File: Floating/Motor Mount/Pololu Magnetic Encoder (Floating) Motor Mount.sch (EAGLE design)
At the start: 1 part

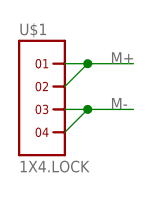
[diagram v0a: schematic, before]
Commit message: Added decoupling capacitor to motor connetions Made 'oval' vias for motors
All in all, should now fit motors
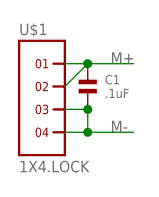
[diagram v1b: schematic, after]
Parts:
- added C1: .1uF, standardparts:CAPACITOR.0603
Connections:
- net M+: now also C1.1
- net M-: now also C1.2
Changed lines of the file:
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@@
 <setting verticaltext="up"/>
 </settings>
-<grid distance="25" unitdist="mil" unit="mil" style="dots" multiple="2" display="yes" altdistance="5" altunitdist="mil" altunit="mil"/>
+<grid distance="0.1" unitdist="inch" unit="inch" style="lines" multiple="1" display="no" altdistance="0.01" altunitdist="inch" altunit="inch"/>
 <layers>
-<layer number="1" name="Top" color="4" fill="1" visible="yes" active="no"/>
-<layer number="16" name="Bottom" color="1" fill="1" visible="yes" active="no"/>
-<layer number="17" name="Pads" color="2" fill="1" visible="yes" active="no"/>
-<layer number="18" name="Vias" color="2" fill="1" visible="yes" active="no"/>
-<layer number="19" name="Unrouted" color="6" fill="1" visible="yes" active="no"/>
-<layer number="20" name="Dimension" color="15" fill="1" visible="yes" active="no"/>
-<layer number="21" name="tPlace" color="7" fill="1" visible="yes" active="no"/>
-<layer number="22" name="bPlace" color="7" fill="1" visible="yes" active="no"/>
-<layer number="23" name="tOrigins" color="15" fill="1" visible="yes" active="no"/>
-<layer number="24" name="bOrigins" color="15" fill="1" visible="yes" active="no"/>
-<layer number="25" name="tNames" color="7" fill="1" visible="yes" active="no"/>
-<layer number="26" name="bNames" color="7" fill="1" visible="yes" active="no"/>
-<layer number="27" name="tValues" color="7" fill="1" visible="yes" active="no"/>
-<layer number="28" name="bValues" color="7" fill="1" visible="yes" active="no"/>
+<layer number="1" name="Top" color="4" fill="1" visible="no" active="no"/>
+<layer number="16" name="Bottom" color="1" fill="1" visible="no" active="no"/>
+<layer number="17" name="Pads" color="2" fill="1" visible="no" active="no"/>
+<layer number="18" name="Vias" color="2" fill="1" visible="no" active="no"/>
+<layer number="19" name="Unrouted" color="6" fill="1" visible="no" active="no"/>
+<layer number="20" name="Dimension" color="15" fill="1" visible="no" active="no"/>
+<layer number="21" name="tPlace" color="7" fill="1" visible="no" active="no"/>
+<layer number="22" name="bPlace" color="7" fill="1" visible="no" active="no"/>
+<layer number="23" name="tOrigins" color="15" fill="1" visible="no" active="no"/>
+<layer number="24" name="bOrigins" color="15" fill="1" visible="no" active="no"/>
+<layer number="25" name="tNames" color="7" fill="1" visible="no" active="no"/>
+<layer number="26" name="bNames" color="7" fill="1" visible="no" active="no"/>
+<layer number="27" name="tValues" color="7" fill="1" visible="no" active="no"/>
+<layer number="28" name="bValues" color="7" fill="1" visible="no" active="no"/>
 <layer number="29" name="tStop" color="7" fill="3" visible="no" active="no"/>
 <layer number="30" name="bStop" color="7" fill="6" visible="no" active="no"/>
@@
 <layer number="35" name="tGlue" color="7" fill="4" visible="no" active="no"/>
 <layer number="36" name="bGlue" color="7" fill="5" visible="no" active="no"/>
-<layer number="37" name="tTest" color="7" fill="1" visible="yes" active="no"/>
-<layer number="38" name="bTest" color="7" fill="1" visible="yes" active="no"/>
+<layer number="37" name="tTest" color="7" fill="1" visible="no" active="no"/>
+<layer number="38" name="bTest" color="7" fill="1" visible="no" active="no"/>
 <layer number="39" name="tKeepout" color="4" fill="11" visible="no" active="no"/>
 <layer number="40" name="bKeepout" color="1" fill="11" visible="no" active="no"/>
@@
 <layer number="44" name="Drills" color="7" fill="1" visible="no" active="no"/>
 <layer number="45" name="Holes" color="7" fill="1" visible="no" active="no"/>
-<layer number="46" name="Milling" color="3" fill="1" visible="yes" active="no"/>
-<layer number="47" name="Measures" color="7" fill="1" visible="yes" active="no"/>
-<layer number="48" name="Document" color="7" fill="1" visible="yes" active="no"/>
-<layer number="49" name="Reference" color="7" fill="1" visible="yes" active="no"/>
-<layer number="50" name="dxf" color="7" fill="1" visible="yes" active="no"/>
-<layer number="51" name="tDocu" color="7" fill="1" visible="yes" active="no"/>
-<layer number="52" name="bDocu" color="7" fill="1" visible="yes" active="no"/>
-<layer number="53" name="tGND_GNDA" color="7" fill="9" visible="yes" active="no"/>
-<layer number="54" name="bGND_GNDA" color="1" fill="9" visible="yes" active="no"/>
-<layer number="56" name="wert" color="7" fill="1" visible="yes" active="no"/>
+<layer number="46" name="Milling" color="3" fill="1" visible="no" active="no"/>
+<layer number="47" name="Measures" color="7" fill="1" visible="no" active="no"/>
+<layer number="48" name="Document" color="7" fill="1" visible="no" active="no"/>
+<layer number="49" name="Reference" color="7" fill="1" visible="no" active="no"/>
+<layer number="50" name="dxf" color="7" fill="1" visible="no" active="no"/>
+<layer number="51" name="tDocu" color="7" fill="1" visible="no" active="no"/>
+<layer number="52" name="bDocu" color="7" fill="1" visible="no" active="no"/>
+<layer number="53" name="tGND_GNDA" color="7" fill="9" visible="no" active="no"/>
+<layer number="54" name="bGND_GNDA" color="1" fill="9" visible="no" active="no"/>
+<layer number="56" name="wert" color="7" fill="1" visible="no" active="no"/>
 <layer number="91" name="Nets" color="2" fill="1" visible="yes" active="yes"/>
 <layer number="92" name="Busses" color="1" fill="1" visible="yes" active="yes"/>
@@
 <part name="U$10" library="thinkmaketest" deviceset="A4_LAYOUT" device=""/>
 <part name="U$1" library="headers(.05in)" deviceset="1X4" device=".LOCK"/>
+<part name="C1" library="standardparts" deviceset="CAPACITOR" device=".0603" value=".1uF"/>
 </parts>
 <sheets>
@@
 <instance part="U$10" gate="G$1" x="0" y="0"/>
 <instance part="U$1" gate="G$1" x="96.52" y="93.98"/>
+<instance part="C1" gate="G$1" x="101.6" y="96.52" rot="R270"/>
 </instances>
 <busses>
@@
 <pinref part="U$1" gate="G$1" pin="1"/>
 <pinref part="U$1" gate="G$1" pin="2"/>
+<pinref part="C1" gate="G$1" pin="1"/>
 </segment>
 </net>
 <net name="M-" class="0">
 <segment>
-<wire x1="99.06" y1="93.98" x2="101.6" y2="93.98" width="0.1524" layer="91"/>
-<wire x1="101.6" y1="93.98" x2="106.68" y2="93.98" width="0.1524" layer="91"/>
-<wire x1="99.06" y1="91.44" x2="101.6" y2="93.98" width="0.1524" layer="91"/>
-<junction x="101.6" y="93.98"/>
-<label x="104.14" y="93.98" size="1.27" layer="95"/>
+<label x="104.14" y="91.44" size="1.27" layer="95"/>
 <pinref part="U$1" gate="G$1" pin="3"/>
 <pinref part="U$1" gate="G$1" pin="4"/>
+<wire x1="106.68" y1="91.44" x2="101.6" y2="91.44" width="0.1524" layer="91"/>
+<wire x1="101.6" y1="91.44" x2="99.06" y2="91.44" width="0.1524" layer="91"/>
+<junction x="101.6" y="91.44"/>
+<pinref part="C1" gate="G$1" pin="2"/>
+<wire x1="101.6" y1="91.44" x2="101.6" y2="93.98" width="0.1524" layer="91"/>
+<wire x1="101.6" y1="93.98" x2="99.06" y2="93.98" width="0.1524" layer="91"/>
+<junction x="101.6" y="93.98"/>
 </segment>
 </net>
